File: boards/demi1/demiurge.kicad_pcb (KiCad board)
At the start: 2 copper layers, 40.1 x 109.9 mm, 155 parts, among them J12 Micro_SD_Card_Det_Hirose_DM3AT, J2 Conn_01x06, U1 MCP6002, U10 TL072, U11 TL072, U13 CH32V307RCT6, U2 AMS1117-3.3, U3 MCP6002, U4 AW20036, U5 W25Q128JVS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

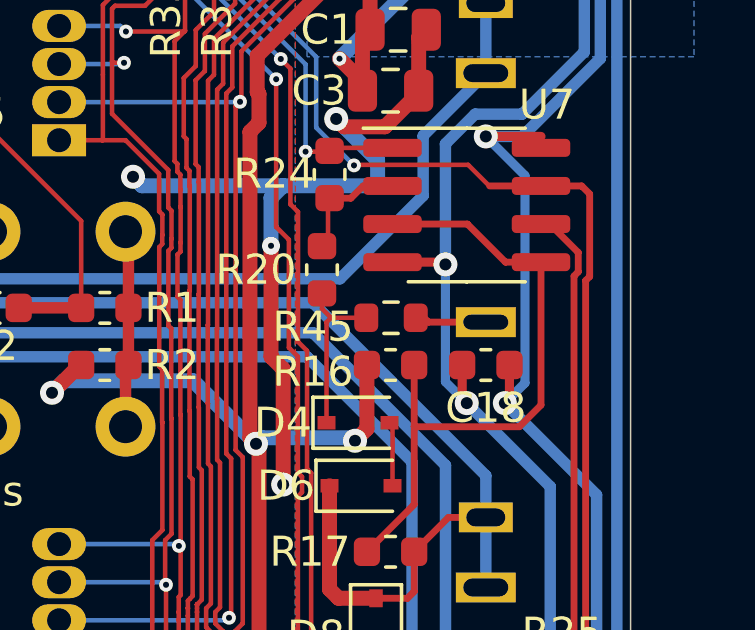
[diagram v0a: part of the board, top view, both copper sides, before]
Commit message: wrong file names on RevG photos.
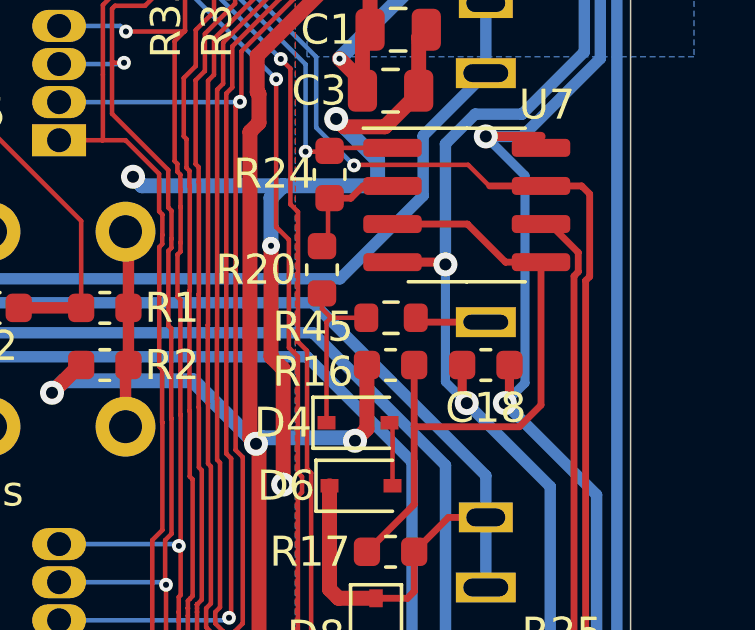
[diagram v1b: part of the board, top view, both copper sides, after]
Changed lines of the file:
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@@
     (pts (xy 116.586 50.8) (xy 76.454 50.8))
     (height 11.049)
-    (gr_text "1.5800 in" (at 96.52 38.601) (layer "Dwgs.User")
+    (gr_text "40.1320 mm" (at 96.52 38.601) (layer "Dwgs.User")
       (effects (font (size 1 1) (thickness 0.15)))
     )
-    (format (units 0) (units_format 1) (precision 4))
+    (format (units 2) (units_format 1) (precision 4))
     (style (thickness 0.15) (arrow_length 1.27) (text_position_mode 0) (extension_height 0.58642) (extension_offset 0) keep_text_aligned)
   )
@@
   )
   (dimension (type aligned) (layer "Dwgs.User")
-    (pts (xy 76.454 160.655) (xy 76.454 50.8))
+    (pts (xy 76.454 162.179) (xy 76.454 60.2996))
     (height -7.453398)
-    (gr_text "109.8550 mm" (at 67.850602 105.7275 90) (layer "Dwgs.User")
+    (gr_text "101.8794 mm" (at 67.850602 111.2393 90) (layer "Dwgs.User")
       (effects (font (size 1 1) (thickness 0.15)))
     )
@@
   (segment (start 92.15 74.55) (end 92.15 83.612401) (width 0.1524) (layer "B.Cu") (net 21))
   (segment (start 92.15 83.612401) (end 92.437599 83.9) (width 0.1524) (layer "B.Cu") (net 21))
-  (segment (start 111.76 90.645) (end 109.8475 90.645) (width 0.2286) (layer "F.Cu") (net 22))
-  (segment (start 109.8475 90.645) (end 109.3725 90.17) (width 0.2286) (layer "F.Cu") (net 22))
+  (segment (start 111.76 90.645) (end 109.57 90.645) (width 0.2286) (layer "F.Cu") (net 22))
+  (segment (start 109.57 90.645) (end 109.3725 90.4475) (width 0.2286) (layer "F.Cu") (net 22))
   (segment (start 99.75 128.42) (end 99.75 126.4625) (width 0.2286) (layer "F.Cu") (net 23))
   (segment (start 99.75 126.4625) (end 99.8475 126.365) (width 0.2286) (layer "F.Cu") (net 23))
